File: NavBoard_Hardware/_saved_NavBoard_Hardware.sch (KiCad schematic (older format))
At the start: 49 parts, among them J1 Conn_Coaxial, U2 ATMEGA328P, U3 OKI, U4 OKI, U5 FGPMMOPA6H, Y1 Crystal

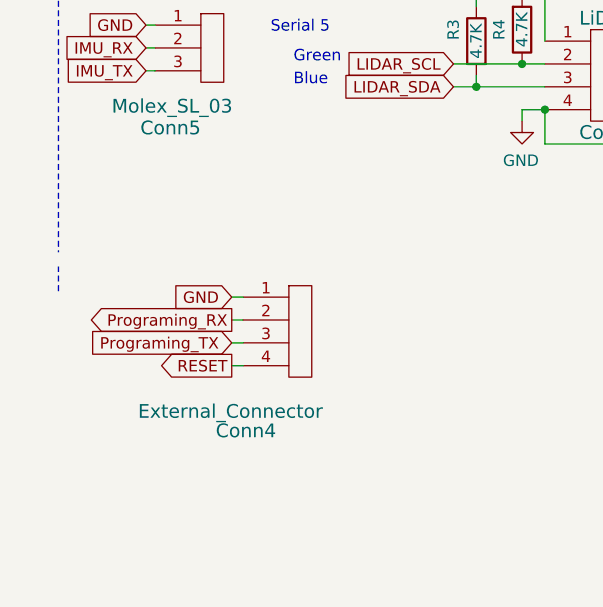
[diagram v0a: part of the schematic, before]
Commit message: Retracing PCB for Rev 2
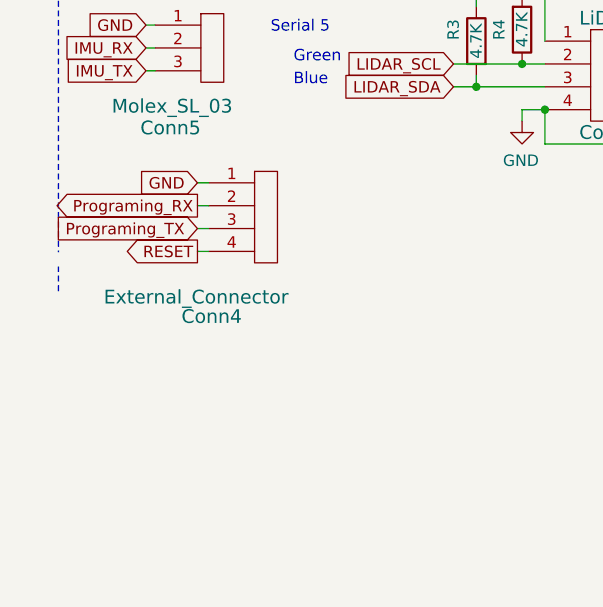
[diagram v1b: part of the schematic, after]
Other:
- moved on the sheet: Conn4
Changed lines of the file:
@@
 L NavBoard_Hardware-rescue:Molex_SL_04-MRDT_Connectors Conn4
 U 1 1 5C74EB18
-P 1480 5520
-F 0 "Conn4" H 1160 5285 60  0000 L CNN
-F 1 "External_Connector" H 820 5370 60  0000 L CNN
-F 2 "MRDT_Connectors:MOLEX_SL_04_Horizontal" H 1480 5520 60  0001 C CNN
-F 3 "" H 1480 5520 60  0001 C CNN
-	1    1480 5520
+P 1330 5020
+F 0 "Conn4" H 1010 4785 60  0000 L CNN
+F 1 "External_Connector" H 670 4870 60  0000 L CNN
+F 2 "MRDT_Connectors:MOLEX_SL_04_Horizontal" H 1330 5020 60  0001 C CNN
+F 3 "" H 1330 5020 60  0001 C CNN
+	1    1330 5020
 	1    0    0    -1
 $EndComp
-Text GLabel 1230 5270 0    50   Output ~ 0
+Text GLabel 1080 4770 0    50   Output ~ 0
 Programing_RX
-Text GLabel 1230 5370 0    50   Input ~ 0
+Text GLabel 1080 4870 0    50   Input ~ 0
 Programing_TX
 Wire Wire Line
-	1280 5270 1230 5270
+	1130 4770 1080 4770
 Wire Wire Line
-	1280 5370 1230 5370
+	1130 4870 1080 4870
 Text GLabel 4535 4260 0    50   Input ~ 0
 RESET
 Wire Wire Line
 	4535 4260 4585 4260
-Text GLabel 1230 5470 0    50   Output ~ 0
+Text GLabel 1080 4970 0    50   Output ~ 0
 RESET
 Wire Wire Line
-	1280 5470 1230 5470
+	1130 4970 1080 4970
 $Comp
 L NavBoard_Hardware-rescue:+3.3V-power #PWR0127
@@
 Wire Notes Line
 	3360 6540 470  6540
-Text GLabel 1230 5170 0    50   Input ~ 0
+Text GLabel 1080 4670 0    50   Input ~ 0
 GND
 Wire Wire Line
-	1230 5170 1280 5170
+	1080 4670 1130 4670
 $Comp
 L NavBoard_Hardware-rescue:C-Device C1
